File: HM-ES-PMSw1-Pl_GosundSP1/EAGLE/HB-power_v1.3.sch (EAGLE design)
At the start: 39 parts, among them IC1 ATMEGA644-10PU, IC4 HLW8012, Q1 16Mhz, T1 BC547, X1 MSTBA2, X2 MSTBA3

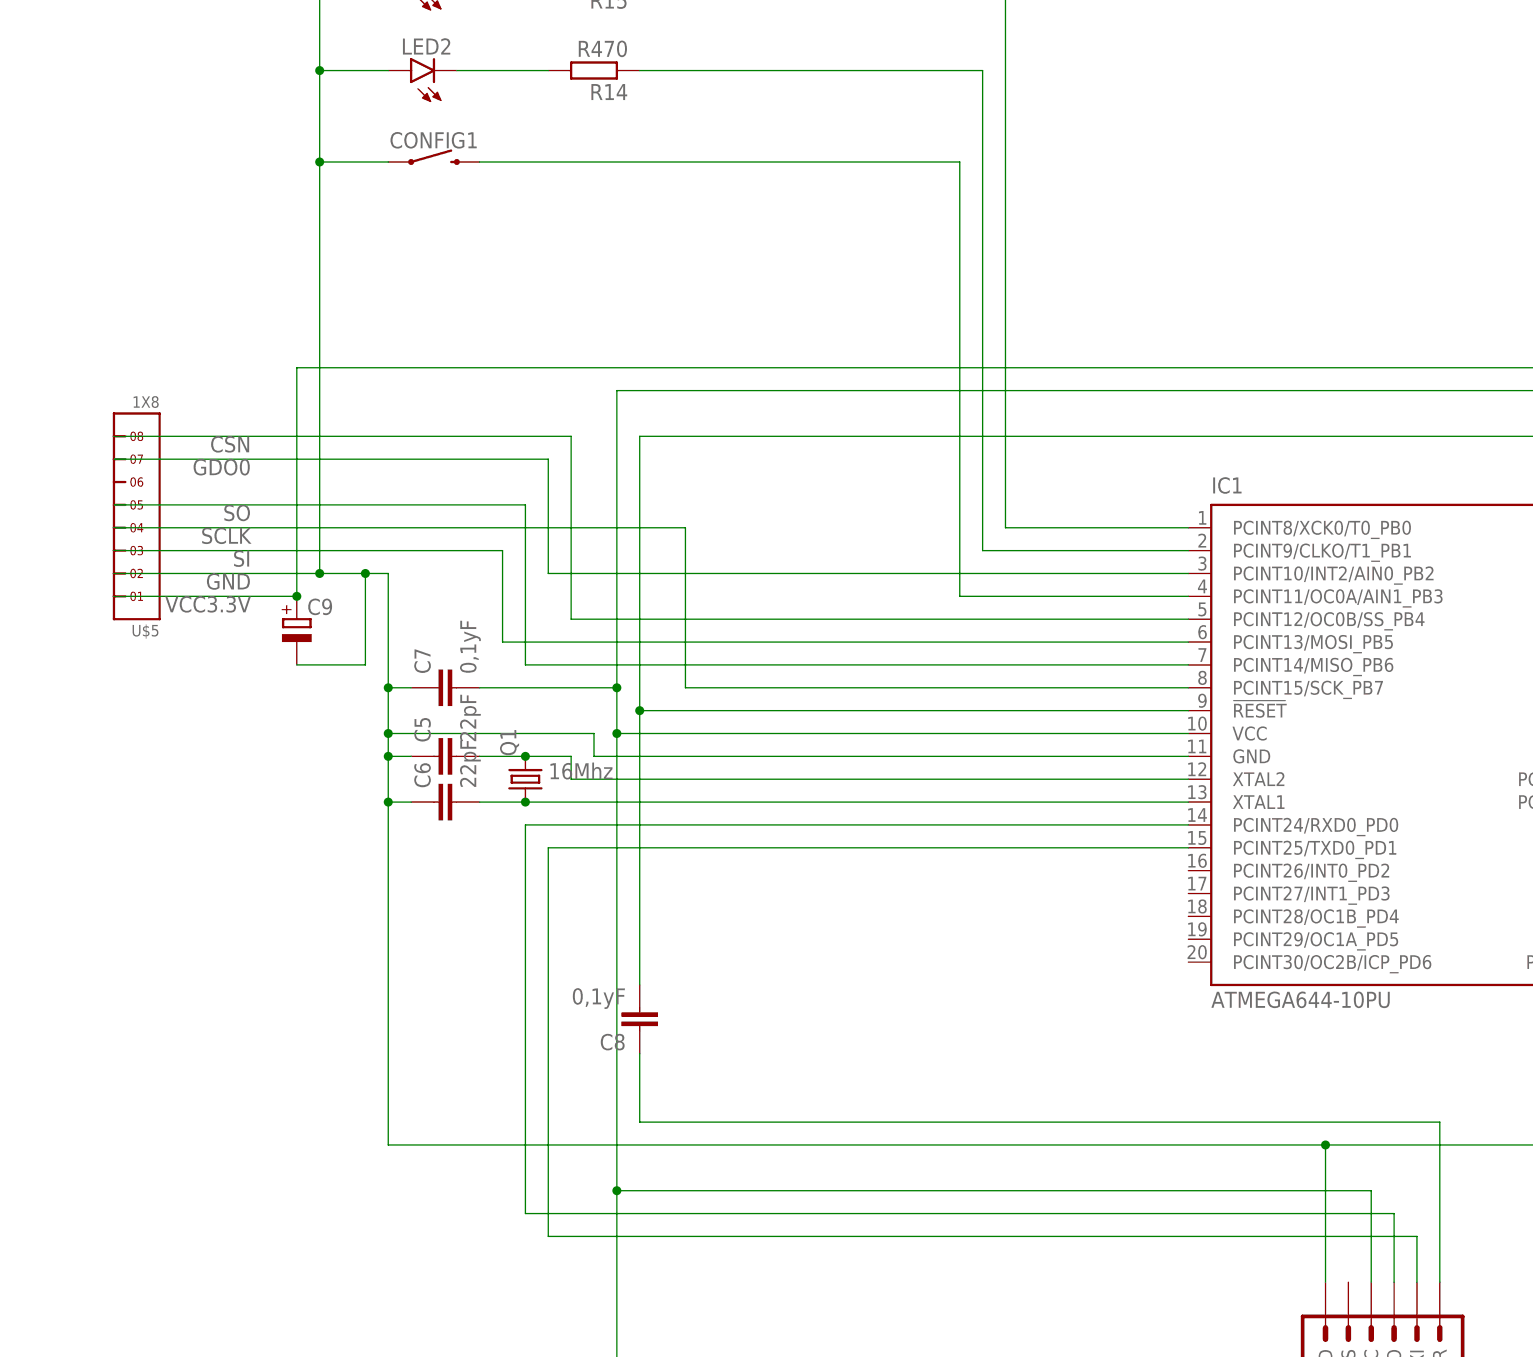
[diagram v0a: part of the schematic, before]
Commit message: Update HB-power_v1.3.sch
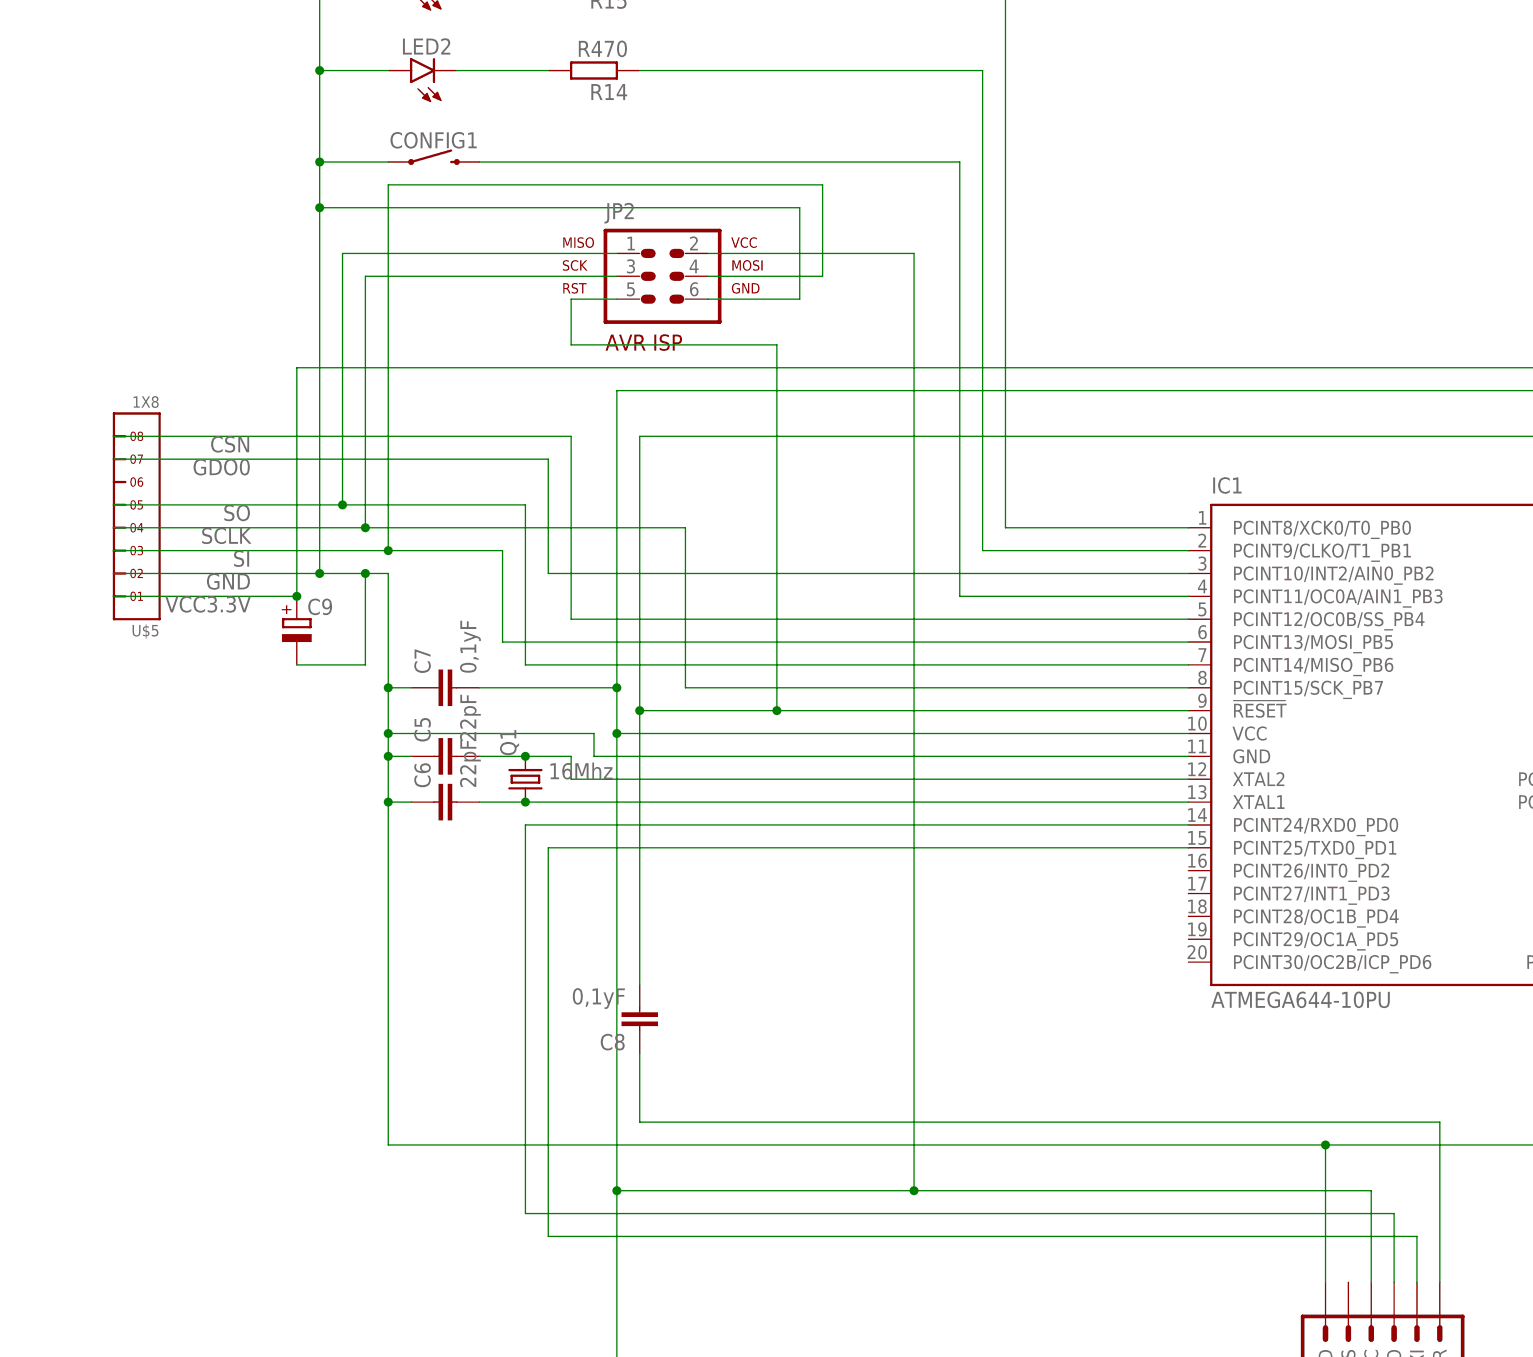
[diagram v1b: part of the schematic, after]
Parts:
- added JP2: AVR-ISP-6VERT, avr-7:AVR-ISP-6VERT
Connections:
- net GND: now also JP2.6
- net N$26: now also JP2.2
- net N$27: now also JP2.5
- net SCLK: now also JP2.3
- net SI: now also JP2.4
- net SO: now also JP2.1
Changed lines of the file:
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@@
 <part name="LED3" library="led" library_urn="urn:adsk.eagle:library:259" deviceset="LED" device="3MM" package3d_urn="urn:adsk.eagle:package:15797/1"/>
 <part name="R15" library="resistor" library_urn="urn:adsk.eagle:library:348" deviceset="R-EU_" device="0309/10" package3d_urn="urn:adsk.eagle:package:23567/1" value="R470"/>
+<part name="JP2" library="avr-7" deviceset="AVR-ISP-6" device="VERT"/>
 </parts>
 <sheets>
@@
 <attribute name="VALUE" x="-57.15" y="320.802" size="1.778" layer="96" rot="R180"/>
 </instance>
+<instance part="JP2" gate="G$1" x="-53.34" y="284.48" smashed="yes">
+<attribute name="NAME" x="-59.69" y="290.83" size="1.778" layer="95" ratio="10"/>
+</instance>
 </instances>
 <busses>
@@
 <pinref part="U$5" gate="G$1" pin="3"/>
 <label x="-99.06" y="254" size="1.778" layer="95" rot="R180"/>
-<wire x1="-114.3" y1="254" x2="-71.12" y2="254" width="0.1524" layer="91"/>
+<wire x1="-114.3" y1="254" x2="-83.82" y2="254" width="0.1524" layer="91"/>
 <pinref part="IC1" gate="G$1" pin="PCINT13/MOSI_PB5"/>
+<wire x1="-83.82" y1="254" x2="-71.12" y2="254" width="0.1524" layer="91"/>
 <wire x1="5.08" y1="243.84" x2="-71.12" y2="243.84" width="0.1524" layer="91"/>
 <wire x1="-71.12" y1="243.84" x2="-71.12" y2="254" width="0.1524" layer="91"/>
+<pinref part="JP2" gate="G$1" pin="4"/>
+<wire x1="-48.26" y1="284.48" x2="-35.56" y2="284.48" width="0.1524" layer="91"/>
+<wire x1="-35.56" y1="284.48" x2="-35.56" y2="294.64" width="0.1524" layer="91"/>
+<wire x1="-35.56" y1="294.64" x2="-83.82" y2="294.64" width="0.1524" layer="91"/>
+<wire x1="-83.82" y1="294.64" x2="-83.82" y2="254" width="0.1524" layer="91"/>
+<junction x="-83.82" y="254"/>
 </segment>
 </net>
@@
 <pinref part="U$5" gate="G$1" pin="5"/>
 <label x="-99.06" y="259.08" size="1.778" layer="95" rot="R180"/>
-<wire x1="-68.58" y1="259.08" x2="-114.3" y2="259.08" width="0.1524" layer="91"/>
+<wire x1="-68.58" y1="259.08" x2="-88.9" y2="259.08" width="0.1524" layer="91"/>
 <pinref part="IC1" gate="G$1" pin="PCINT14/MISO_PB6"/>
+<wire x1="-88.9" y1="259.08" x2="-114.3" y2="259.08" width="0.1524" layer="91"/>
 <wire x1="-68.58" y1="259.08" x2="-68.58" y2="241.3" width="0.1524" layer="91"/>
 <wire x1="-68.58" y1="241.3" x2="5.08" y2="241.3" width="0.1524" layer="91"/>
+<pinref part="JP2" gate="G$1" pin="1"/>
+<wire x1="-58.42" y1="287.02" x2="-88.9" y2="287.02" width="0.1524" layer="91"/>
+<wire x1="-88.9" y1="287.02" x2="-88.9" y2="259.08" width="0.1524" layer="91"/>
+<junction x="-88.9" y="259.08"/>
 </segment>
 </net>
@@
 <pinref part="U$5" gate="G$1" pin="4"/>
 <label x="-99.06" y="256.54" size="1.778" layer="95" rot="R180"/>
-<wire x1="-50.8" y1="256.54" x2="-114.3" y2="256.54" width="0.1524" layer="91"/>
+<wire x1="-50.8" y1="256.54" x2="-86.36" y2="256.54" width="0.1524" layer="91"/>
 <pinref part="IC1" gate="G$1" pin="PCINT15/SCK_PB7"/>
+<wire x1="-86.36" y1="256.54" x2="-114.3" y2="256.54" width="0.1524" layer="91"/>
 <wire x1="5.08" y1="238.76" x2="-50.8" y2="238.76" width="0.1524" layer="91"/>
 <wire x1="-50.8" y1="238.76" x2="-50.8" y2="256.54" width="0.1524" layer="91"/>
+<pinref part="JP2" gate="G$1" pin="3"/>
+<wire x1="-58.42" y1="284.48" x2="-86.36" y2="284.48" width="0.1524" layer="91"/>
+<wire x1="-86.36" y1="284.48" x2="-86.36" y2="256.54" width="0.1524" layer="91"/>
+<junction x="-86.36" y="256.54"/>
 </segment>
 </net>
@@
 <pinref part="J1" gate="G$1" pin="VCC"/>
 <wire x1="25.4" y1="172.72" x2="25.4" y2="182.88" width="0.1524" layer="91"/>
-<wire x1="25.4" y1="182.88" x2="-58.42" y2="182.88" width="0.1524" layer="91"/>
+<wire x1="25.4" y1="182.88" x2="-25.4" y2="182.88" width="0.1524" layer="91"/>
 <junction x="-58.42" y="182.88"/>
 <pinref part="JP1" gate="1" pin="1"/>
+<wire x1="-25.4" y1="182.88" x2="-58.42" y2="182.88" width="0.1524" layer="91"/>
 <wire x1="162.56" y1="147.32" x2="134.62" y2="147.32" width="0.1524" layer="91"/>
 <wire x1="134.62" y1="147.32" x2="134.62" y2="124.46" width="0.1524" layer="91"/>
 <junction x="134.62" y="124.46"/>
+<pinref part="JP2" gate="G$1" pin="2"/>
+<wire x1="-48.26" y1="287.02" x2="-25.4" y2="287.02" width="0.1524" layer="91"/>
+<wire x1="-25.4" y1="287.02" x2="-25.4" y2="182.88" width="0.1524" layer="91"/>
+<junction x="-25.4" y="182.88"/>
 </segment>
 </net>
@@
 <pinref part="IC1" gate="G$1" pin="!RESET"/>
 <wire x1="-55.88" y1="266.7" x2="-55.88" y2="236.22" width="0.1524" layer="91"/>
-<wire x1="-55.88" y1="236.22" x2="5.08" y2="236.22" width="0.1524" layer="91"/>
+<wire x1="-55.88" y1="236.22" x2="-40.64" y2="236.22" width="0.1524" layer="91"/>
 <pinref part="C8" gate="G$1" pin="2"/>
+<wire x1="-40.64" y1="236.22" x2="5.08" y2="236.22" width="0.1524" layer="91"/>
 <wire x1="-55.88" y1="236.22" x2="-55.88" y2="205.74" width="0.1524" layer="91"/>
 <junction x="-55.88" y="236.22"/>
+<pinref part="JP2" gate="G$1" pin="5"/>
+<wire x1="-58.42" y1="281.94" x2="-63.5" y2="281.94" width="0.1524" layer="91"/>
+<wire x1="-63.5" y1="281.94" x2="-63.5" y2="276.86" width="0.1524" layer="91"/>
+<wire x1="-63.5" y1="276.86" x2="-40.64" y2="276.86" width="0.1524" layer="91"/>
+<wire x1="-40.64" y1="276.86" x2="-40.64" y2="236.22" width="0.1524" layer="91"/>
+<junction x="-40.64" y="236.22"/>
 </segment>
 </net>
@@
 <wire x1="-83.82" y1="251.46" x2="-83.82" y2="238.76" width="0.1524" layer="91"/>
 <junction x="-83.82" y="238.76"/>
-<wire x1="-91.44" y1="297.18" x2="-91.44" y2="251.46" width="0.1524" layer="91"/>
+<wire x1="-91.44" y1="297.18" x2="-91.44" y2="292.1" width="0.1524" layer="91"/>
 <junction x="-91.44" y="251.46"/>
+<wire x1="-91.44" y1="292.1" x2="-91.44" y2="251.46" width="0.1524" layer="91"/>
 <wire x1="-91.44" y1="317.5" x2="-91.44" y2="307.34" width="0.1524" layer="91"/>
 <wire x1="-91.44" y1="307.34" x2="-91.44" y2="297.18" width="0.1524" layer="91"/>
@@
 <pinref part="U$5" gate="G$1" pin="2"/>
 <junction x="20.32" y="187.96"/>
-</segment>
-</net>
+<pinref part="JP2" gate="G$1" pin="6"/>
+<wire x1="-48.26" y1="281.94" x2="-38.1" y2="281.94" width="0.1524" layer="91"/>
+<wire x1="-38.1" y1="281.94" x2="-38.1" y2="292.1" width="0.1524" layer="91"/>
+<wire x1="-38.1" y1="292.1" x2="-91.44" y2="292.1" width="0.1524" layer="91"/>
+<junction x="-91.44" y="292.1"/>
+</segment>
+</net>
